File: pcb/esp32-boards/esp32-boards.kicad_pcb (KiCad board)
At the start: 2 copper layers, 55 x 42 mm, 53 parts, among them J1 LCD, J2 USB_B_Micro, J3 BATTERY, Q1 Q_Photo_NPN, SW1 BOOT_MODE, SW2 START, SW3 RESET, SW4 BATTERY_EN, U1 ESP32-C3-WROOM-02, U2 MAX40200AUK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

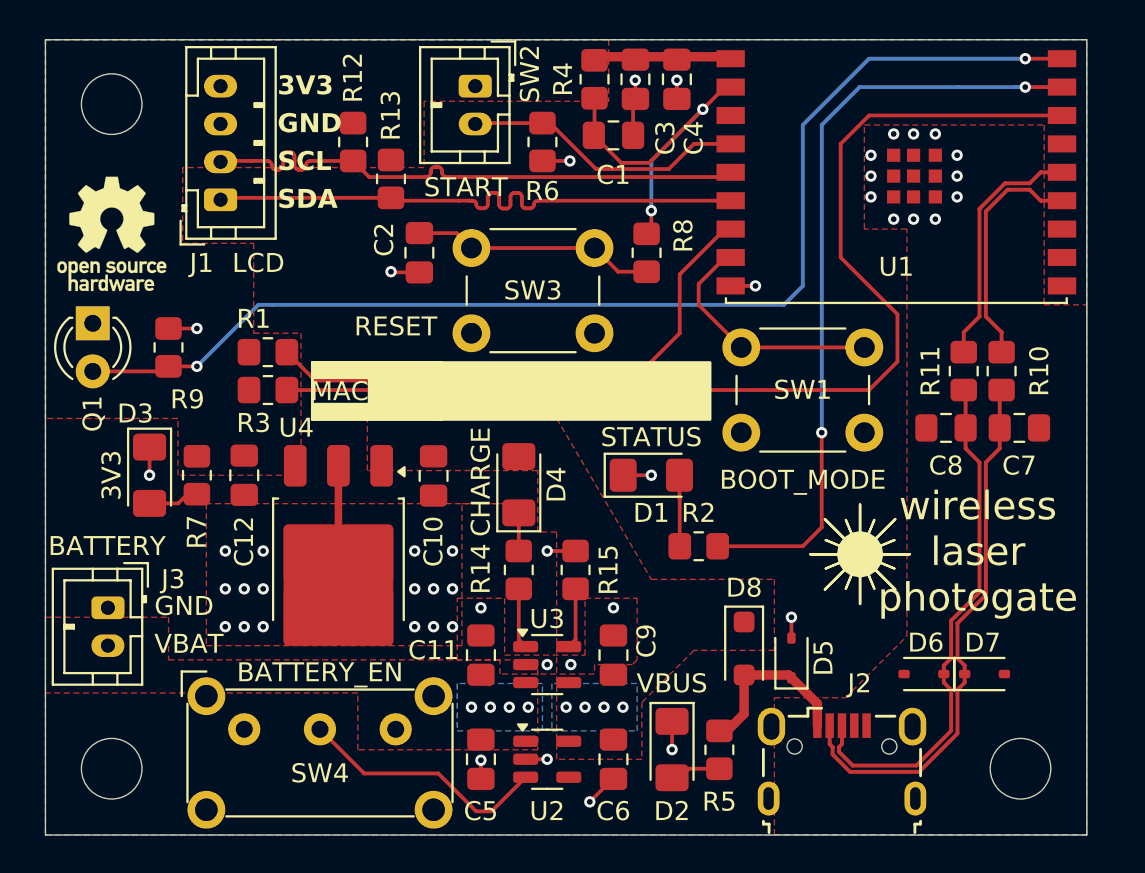
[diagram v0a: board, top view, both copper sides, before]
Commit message: add tooling holes for assembly
https://jlcpcb.com/help/article/47-How-to-add-tooling-holes-for-PCB-assembly-order
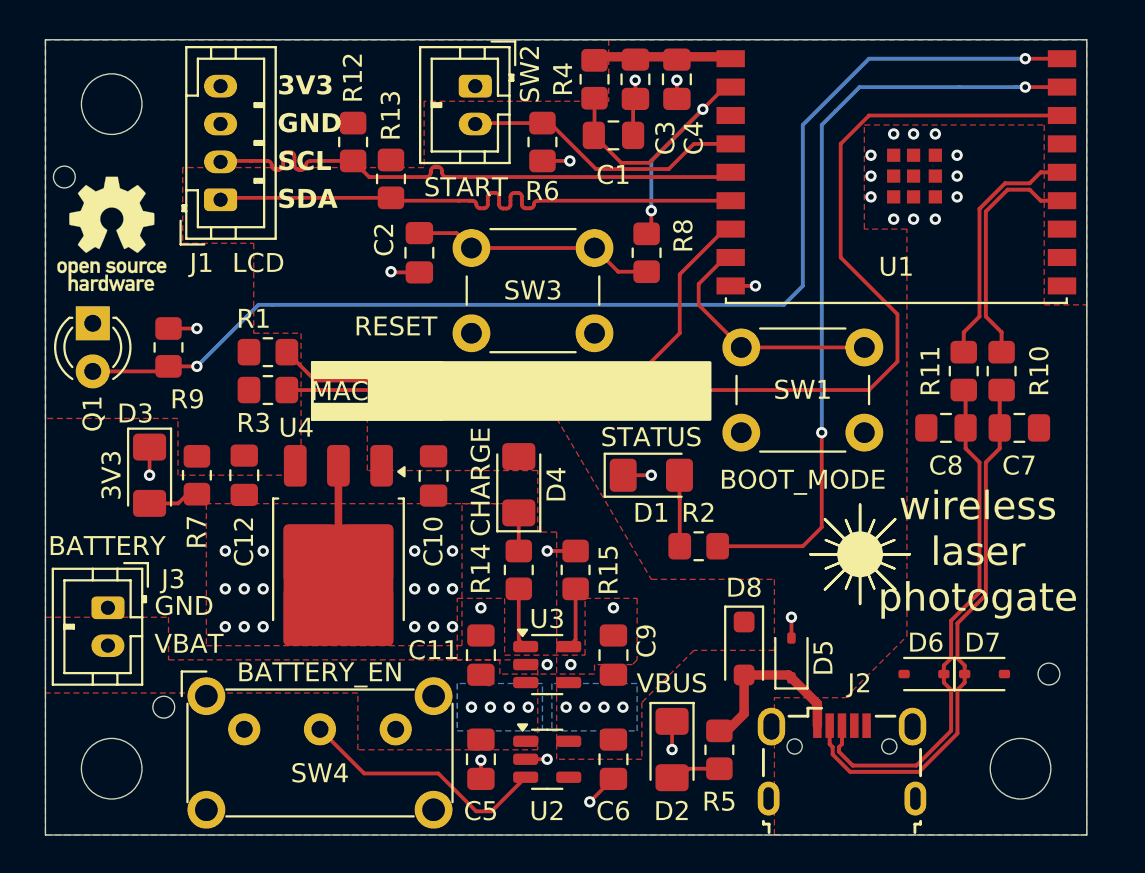
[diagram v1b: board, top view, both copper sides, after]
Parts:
- added REF**: tooling_hole, laser-photogate:tooling_hole, F.Cu at (185.8, 130.5)
- added REF**: tooling_hole, laser-photogate:tooling_hole, F.Cu at (180.5, 102.5)
- added REF**: tooling_hole, laser-photogate:tooling_hole, F.Cu at (232.5, 128.8)

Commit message: remove tooling holes; finalize for production
It's easier to have JLC add the tooling holes.
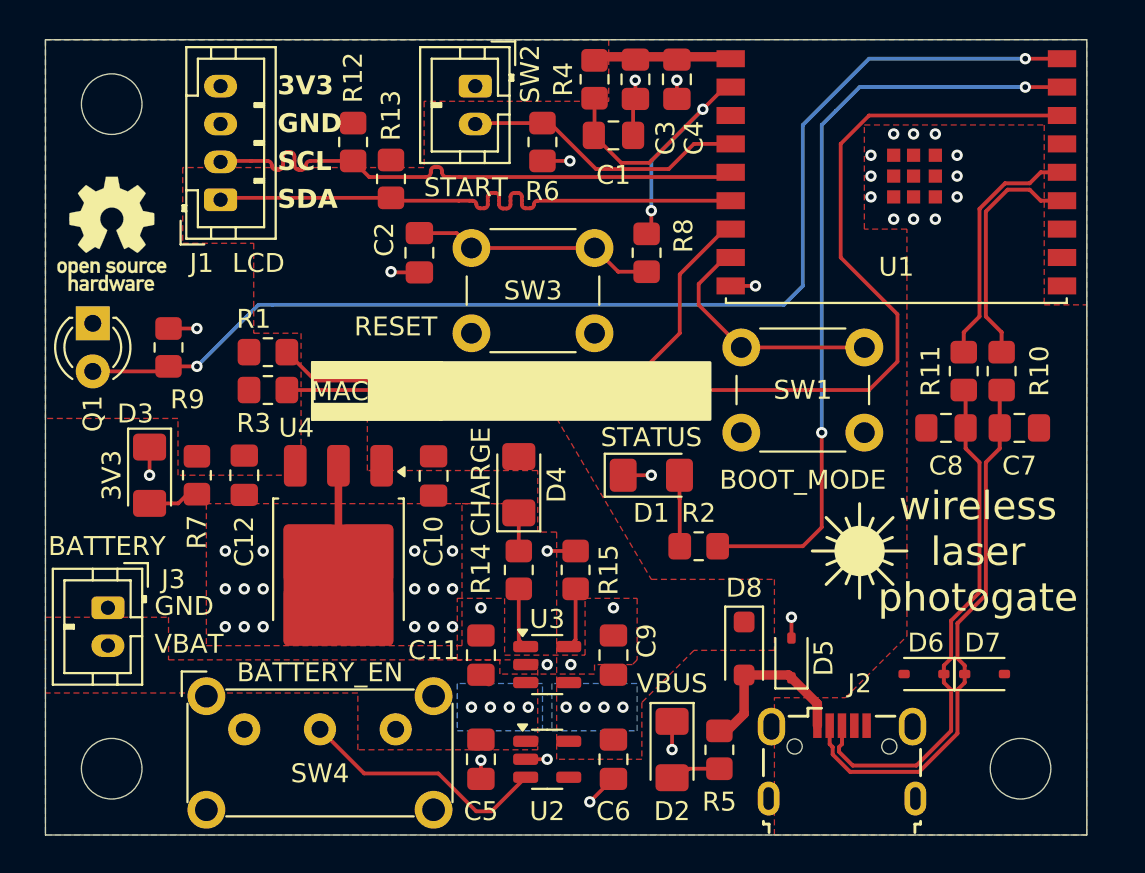
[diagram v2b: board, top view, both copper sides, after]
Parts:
- removed the REF** at (185.8, 130.5)
- removed the REF** at (180.5, 102.5)
- removed the REF** at (232.5, 128.8)
- moved svg2mod 3.66 mm to (222.5, 122.2)
